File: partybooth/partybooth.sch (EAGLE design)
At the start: 21 parts, among them IC1 TINY13-20PU, IC2 78L05Z, J1 Lamp, J2 Button, J3 12V, T1 2N3904, T2 2N3904, X1 1501_06

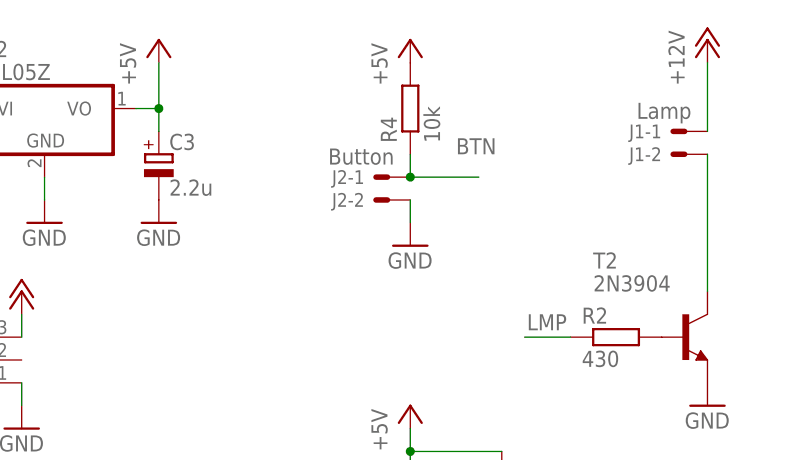
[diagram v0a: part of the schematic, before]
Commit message: 
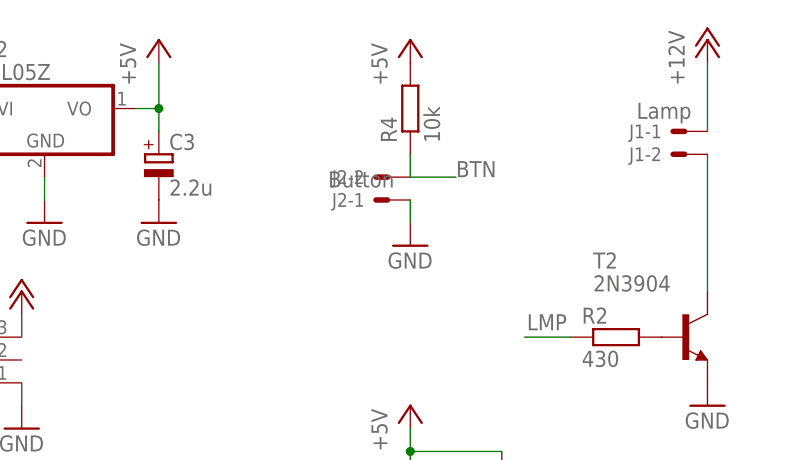
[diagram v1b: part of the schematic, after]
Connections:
- net BTN: now also J2-2.S; no longer J2-1.S
- net GND: now also J2-1.S; no longer J2-2.S
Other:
- moved on the sheet: J2-1, J2-2
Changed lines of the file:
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@@
 <instance part="OK1" gate="A" x="38.1" y="45.72"/>
 <instance part="OK1" gate="B" x="38.1" y="30.48"/>
-<instance part="J2" gate="-1" x="-17.78" y="96.52" rot="MR0"/>
-<instance part="J2" gate="-2" x="-17.78" y="93.98" rot="MR0"/>
+<instance part="J2" gate="-1" x="-17.78" y="93.98" rot="MR0"/>
+<instance part="J2" gate="-2" x="-17.78" y="96.52" rot="MR0"/>
 <instance part="SV1" gate="1" x="5.08" y="48.26" rot="R180"/>
 <instance part="P+4" gate="1" x="15.24" y="58.42"/>
@@
 </segment>
 <segment>
-<pinref part="GND10" gate="1" pin="GND"/>
-<pinref part="J2" gate="-2" pin="S"/>
-<wire x1="-15.24" y1="91.44" x2="-15.24" y2="93.98" width="0.1524" layer="91"/>
-</segment>
-<segment>
 <pinref part="GND11" gate="1" pin="GND"/>
 <pinref part="J3" gate="G$1" pin="1"/>
 <wire x1="-58.42" y1="73.66" x2="-58.42" y2="71.12" width="0.1524" layer="91"/>
+</segment>
+<segment>
+<pinref part="J2" gate="-1" pin="S"/>
+<pinref part="GND10" gate="1" pin="GND"/>
+<wire x1="-15.24" y1="93.98" x2="-15.24" y2="91.44" width="0.1524" layer="91"/>
 </segment>
 </net>
@@
 <net name="BTN" class="0">
 <segment>
-<pinref part="R4" gate="G$1" pin="1"/>
-<wire x1="-15.24" y1="96.52" x2="-15.24" y2="99.06" width="0.1524" layer="91"/>
-<pinref part="J2" gate="-1" pin="S"/>
-<wire x1="-15.24" y1="96.52" x2="-7.62" y2="96.52" width="0.1524" layer="91"/>
-<label x="-10.16" y="99.06" size="1.778" layer="95"/>
-<junction x="-15.24" y="96.52"/>
-</segment>
-<segment>
 <pinref part="IC1" gate="G$1" pin="PB1/PCINT1/AIN1/OC0B/INT0/MISO"/>
 <pinref part="SV1" gate="1" pin="1"/>
@@
 <label x="-15.24" y="51.308" size="1.778" layer="95"/>
 </segment>
-</net>
+<segment>
+<pinref part="R4" gate="G$1" pin="1"/>
+<pinref part="J2" gate="-2" pin="S"/>
+<wire x1="-15.24" y1="99.06" x2="-15.24" y2="96.52" width="0.1524" layer="91"/>
+<wire x1="-15.24" y1="96.52" x2="-10.16" y2="96.52" width="0.1524" layer="91"/>
+<label x="-10.16" y="96.52" size="1.778" layer="95"/>
+</segment>
+</net>

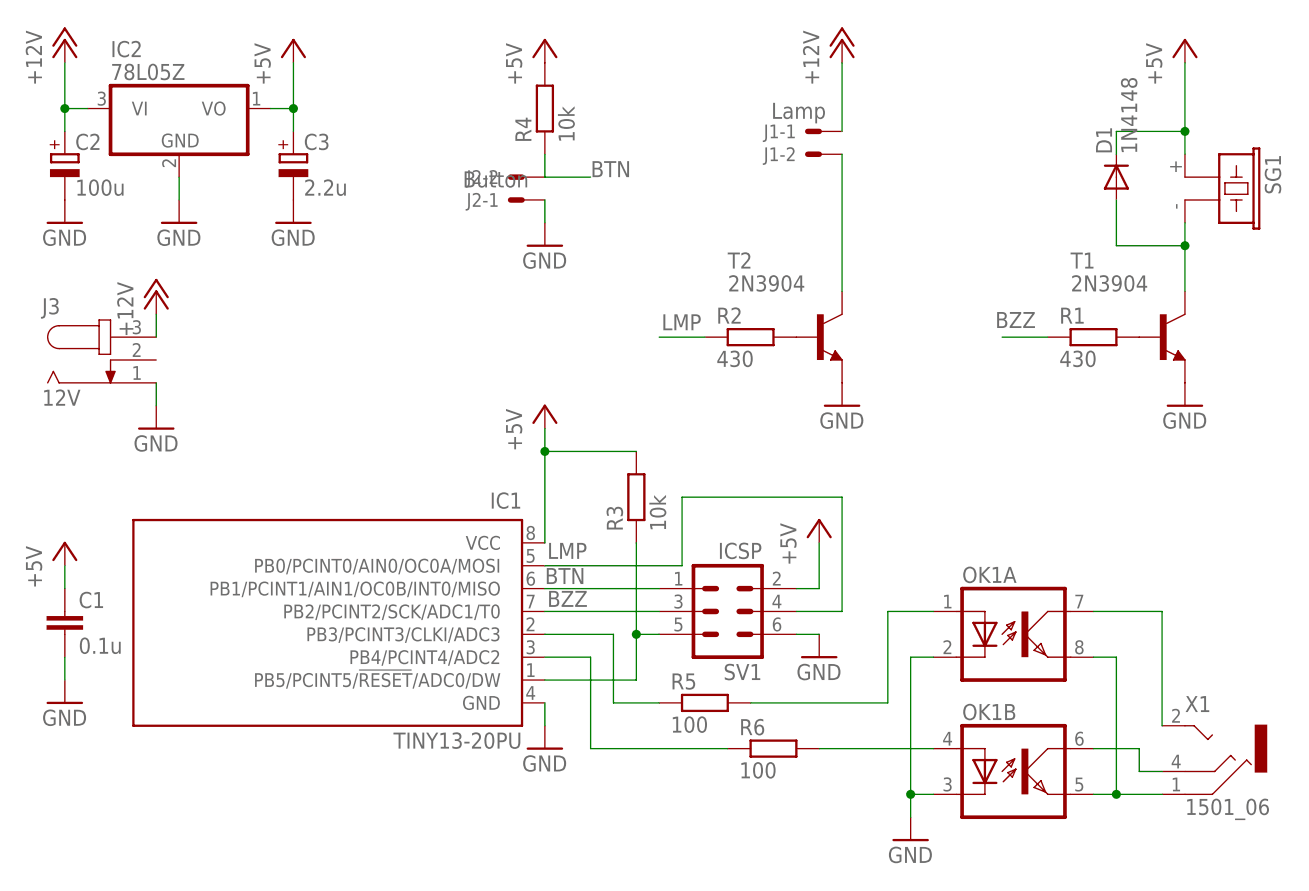
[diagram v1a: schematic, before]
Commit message: 
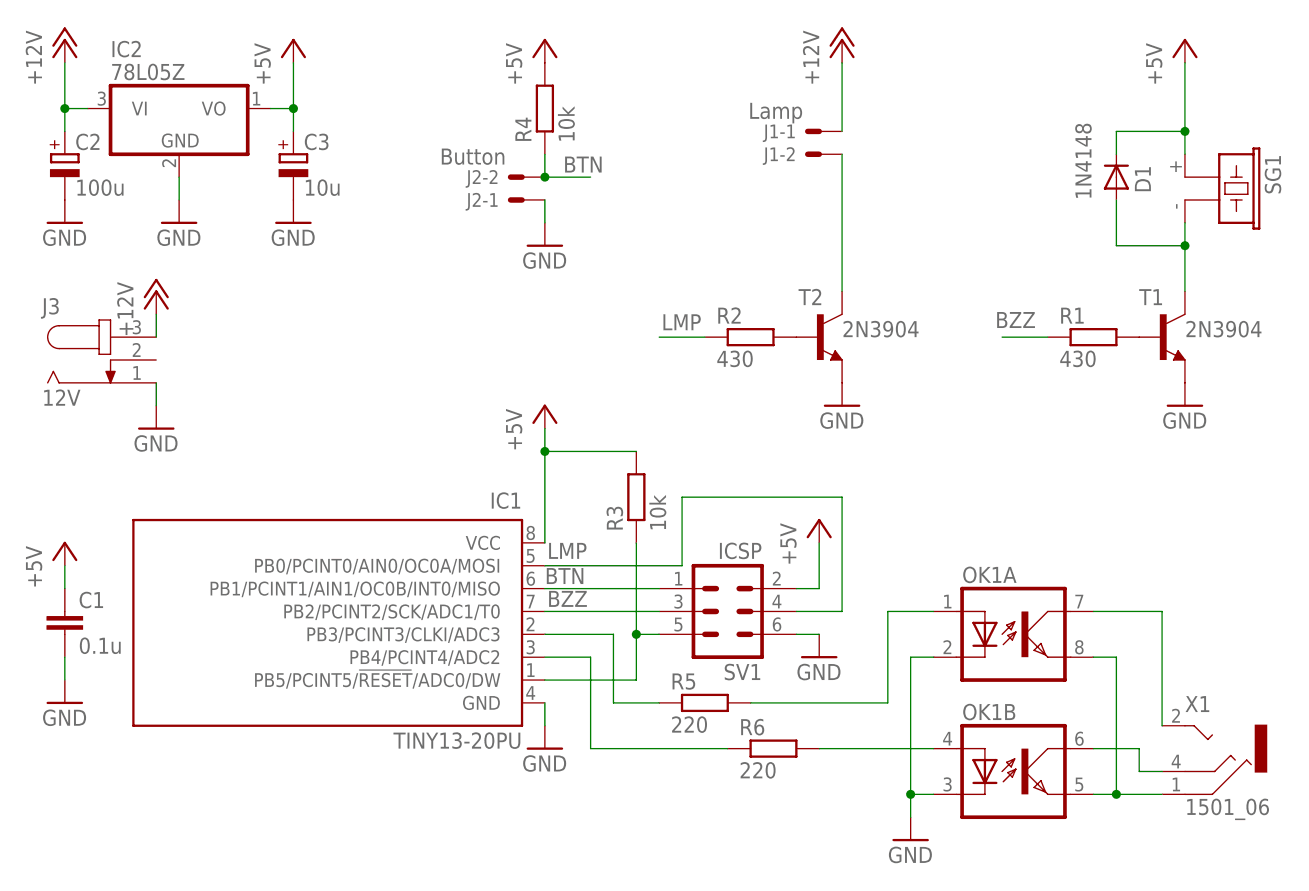
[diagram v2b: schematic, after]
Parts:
- C3: value 2.2u -> 10u
- R5, R6: value 100 -> 220
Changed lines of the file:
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@@
 <layer number="95" name="Names" color="7" fill="1" visible="yes" active="yes"/>
 <layer number="96" name="Values" color="7" fill="1" visible="yes" active="yes"/>
-<layer number="97" name="Info" color="7" fill="1" visible="yes" active="yes"/>
+<layer number="97" name="Info" color="7" fill="1" visible="no" active="yes"/>
 <layer number="98" name="Guide" color="6" fill="1" visible="yes" active="yes"/>
 </layers>
@@
 <part name="IC2" library="linear" deviceset="78*" device="Z" technology="L05"/>
 <part name="C2" library="rcl" deviceset="CPOL-EU" device="B45181B" value="100u"/>
-<part name="C3" library="rcl" deviceset="CPOL-EU" device="B45181B" value="2.2u"/>
+<part name="C3" library="rcl" deviceset="CPOL-EU" device="B45181B" value="10u"/>
 <part name="GND7" library="supply1" deviceset="GND" device=""/>
 <part name="GND8" library="supply1" deviceset="GND" device=""/>
@@
 <part name="P+8" library="supply1" deviceset="+5V" device=""/>
 <part name="GND10" library="supply1" deviceset="GND" device=""/>
-<part name="R5" library="rcl" deviceset="R-EU_" device="0204/7" value="100"/>
-<part name="R6" library="rcl" deviceset="R-EU_" device="0204/7" value="100"/>
+<part name="R5" library="rcl" deviceset="R-EU_" device="0204/7" value="220"/>
+<part name="R6" library="rcl" deviceset="R-EU_" device="0204/7" value="220"/>
 <part name="J3" library="con-jack" deviceset="JACK-PLUG" device="0" value="12V"/>
 <part name="P+9" library="supply1" deviceset="+12V" device=""/>
@@
 <instances>
 <instance part="SG1" gate="G$1" x="58.42" y="96.52" rot="R270"/>
-<instance part="T1" gate="G1" x="53.34" y="78.74"/>
-<instance part="T2" gate="G1" x="15.24" y="78.74"/>
+<instance part="T1" gate="G1" x="53.34" y="78.74" smashed="yes">
+<attribute name="NAME" x="50.8" y="82.296" size="1.778" layer="95"/>
+<attribute name="VALUE" x="55.88" y="78.74" size="1.778" layer="96"/>
+</instance>
+<instance part="T2" gate="G1" x="15.24" y="78.74" smashed="yes">
+<attribute name="NAME" x="12.954" y="82.296" size="1.778" layer="95"/>
+<attribute name="VALUE" x="17.78" y="78.74" size="1.778" layer="96"/>
+</instance>
 <instance part="R1" gate="G$1" x="45.72" y="78.74"/>
 <instance part="GND1" gate="1" x="55.88" y="71.12"/>
 <instance part="P+1" gate="1" x="55.88" y="111.76"/>
-<instance part="D1" gate="G$1" x="48.26" y="96.52" rot="R90"/>
-<instance part="J1" gate="-1" x="15.24" y="101.6" rot="MR0"/>
+<instance part="D1" gate="G$1" x="48.26" y="96.52" smashed="yes" rot="R90">
+<attribute name="NAME" x="52.0954" y="94.742" size="1.778" layer="95" rot="R90"/>
+<attribute name="VALUE" x="45.4914" y="93.98" size="1.778" layer="96" rot="R90"/>
+</instance>
+<instance part="J1" gate="-1" x="15.24" y="101.6" smashed="yes" rot="MR0">
+<attribute name="NAME" x="12.7" y="100.838" size="1.524" layer="95" rot="MR0"/>
+<attribute name="VALUE" x="13.462" y="102.997" size="1.778" layer="96" rot="MR0"/>
+</instance>
 <instance part="J1" gate="-2" x="15.24" y="99.06" rot="MR0"/>
 <instance part="P+2" gate="1" x="17.78" y="111.76"/>
@@
 <instance part="OK1" gate="A" x="38.1" y="45.72"/>
 <instance part="OK1" gate="B" x="38.1" y="30.48"/>
-<instance part="J2" gate="-1" x="-17.78" y="93.98" rot="MR0"/>
+<instance part="J2" gate="-1" x="-17.78" y="93.98" smashed="yes" rot="MR0">
+<attribute name="NAME" x="-20.32" y="93.218" size="1.524" layer="95" rot="MR0"/>
+<attribute name="VALUE" x="-19.558" y="97.917" size="1.778" layer="96" rot="MR0"/>
+</instance>
 <instance part="J2" gate="-2" x="-17.78" y="96.52" rot="MR0"/>
 <instance part="SV1" gate="1" x="5.08" y="48.26" rot="R180"/>
@@
 <pinref part="R4" gate="G$1" pin="1"/>
 <pinref part="J2" gate="-2" pin="S"/>
-<wire x1="-15.24" y1="99.06" x2="-15.24" y2="96.52" width="0.1524" layer="91"/>
 <wire x1="-15.24" y1="96.52" x2="-10.16" y2="96.52" width="0.1524" layer="91"/>
-<label x="-10.16" y="96.52" size="1.778" layer="95"/>
-</segment>
-</net>
+<label x="-13.208" y="97.028" size="1.778" layer="95"/>
+<junction x="-15.24" y="96.52"/>
+<wire x1="-15.24" y1="96.52" x2="-15.24" y2="99.06" width="0.1524" layer="91"/>
+</segment>
+</net>

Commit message: 
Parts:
- C1: device rcl:C-EU025_050-025X075 -> rcl:C-EU050-025X075
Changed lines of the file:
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@@
 <grid distance="0.1" unitdist="inch" unit="inch" style="lines" multiple="1" display="no" altdistance="0.01" altunitdist="inch" altunit="inch"/>
 <layers>
-<layer number="1" name="Top" color="4" fill="1" visible="no" active="no"/>
-<layer number="2" name="Route2" color="1" fill="3" visible="no" active="no"/>
-<layer number="3" name="Route3" color="4" fill="3" visible="no" active="no"/>
-<layer number="14" name="Route14" color="1" fill="6" visible="no" active="no"/>
-<layer number="15" name="Route15" color="4" fill="6" visible="no" active="no"/>
-<layer number="16" name="Bottom" color="1" fill="1" visible="no" active="no"/>
-<layer number="17" name="Pads" color="2" fill="1" visible="no" active="no"/>
-<layer number="18" name="Vias" color="2" fill="1" visible="no" active="no"/>
-<layer number="19" name="Unrouted" color="6" fill="1" visible="no" active="no"/>
-<layer number="20" name="Dimension" color="15" fill="1" visible="no" active="no"/>
-<layer number="21" name="tPlace" color="7" fill="1" visible="no" active="no"/>
-<layer number="22" name="bPlace" color="7" fill="1" visible="no" active="no"/>
-<layer number="23" name="tOrigins" color="15" fill="1" visible="no" active="no"/>
-<layer number="24" name="bOrigins" color="15" fill="1" visible="no" active="no"/>
-<layer number="25" name="tNames" color="7" fill="1" visible="no" active="no"/>
-<layer number="26" name="bNames" color="7" fill="1" visible="no" active="no"/>
-<layer number="27" name="tValues" color="7" fill="1" visible="no" active="no"/>
-<layer number="28" name="bValues" color="7" fill="1" visible="no" active="no"/>
+<layer number="1" name="Top" color="4" fill="1" visible="yes" active="no"/>
+<layer number="2" name="Route2" color="1" fill="3" visible="yes" active="no"/>
+<layer number="3" name="Route3" color="4" fill="3" visible="yes" active="no"/>
+<layer number="14" name="Route14" color="1" fill="6" visible="yes" active="no"/>
+<layer number="15" name="Route15" color="4" fill="6" visible="yes" active="no"/>
+<layer number="16" name="Bottom" color="1" fill="1" visible="yes" active="no"/>
+<layer number="17" name="Pads" color="2" fill="1" visible="yes" active="no"/>
+<layer number="18" name="Vias" color="2" fill="1" visible="yes" active="no"/>
+<layer number="19" name="Unrouted" color="6" fill="1" visible="yes" active="no"/>
+<layer number="20" name="Dimension" color="15" fill="1" visible="yes" active="no"/>
+<layer number="21" name="tPlace" color="7" fill="1" visible="yes" active="no"/>
+<layer number="22" name="bPlace" color="7" fill="1" visible="yes" active="no"/>
+<layer number="23" name="tOrigins" color="15" fill="1" visible="yes" active="no"/>
+<layer number="24" name="bOrigins" color="15" fill="1" visible="yes" active="no"/>
+<layer number="25" name="tNames" color="7" fill="1" visible="yes" active="no"/>
+<layer number="26" name="bNames" color="7" fill="1" visible="yes" active="no"/>
+<layer number="27" name="tValues" color="7" fill="1" visible="yes" active="no"/>
+<layer number="28" name="bValues" color="7" fill="1" visible="yes" active="no"/>
 <layer number="29" name="tStop" color="7" fill="3" visible="no" active="no"/>
 <layer number="30" name="bStop" color="7" fill="6" visible="no" active="no"/>
@@
 <layer number="35" name="tGlue" color="7" fill="4" visible="no" active="no"/>
 <layer number="36" name="bGlue" color="7" fill="5" visible="no" active="no"/>
-<layer number="37" name="tTest" color="7" fill="1" visible="no" active="no"/>
-<layer number="38" name="bTest" color="7" fill="1" visible="no" active="no"/>
+<layer number="37" name="tTest" color="7" fill="1" visible="yes" active="no"/>
+<layer number="38" name="bTest" color="7" fill="1" visible="yes" active="no"/>
 <layer number="39" name="tKeepout" color="4" fill="11" visible="no" active="no"/>
 <layer number="40" name="bKeepout" color="1" fill="11" visible="no" active="no"/>
@@
 <layer number="44" name="Drills" color="7" fill="1" visible="no" active="no"/>
 <layer number="45" name="Holes" color="7" fill="1" visible="no" active="no"/>
-<layer number="46" name="Milling" color="3" fill="1" visible="no" active="no"/>
-<layer number="47" name="Measures" color="7" fill="1" visible="no" active="no"/>
-<layer number="48" name="Document" color="7" fill="1" visible="no" active="no"/>
-<layer number="49" name="Reference" color="7" fill="1" visible="no" active="no"/>
-<layer number="51" name="tDocu" color="6" fill="1" visible="no" active="no"/>
-<layer number="52" name="bDocu" color="7" fill="1" visible="no" active="no"/>
+<layer number="46" name="Milling" color="3" fill="1" visible="yes" active="no"/>
+<layer number="47" name="Measures" color="7" fill="1" visible="yes" active="no"/>
+<layer number="48" name="Document" color="7" fill="1" visible="yes" active="no"/>
+<layer number="49" name="Reference" color="7" fill="1" visible="yes" active="no"/>
+<layer number="51" name="tDocu" color="7" fill="1" visible="yes" active="no"/>
+<layer number="52" name="bDocu" color="7" fill="1" visible="yes" active="no"/>
 <layer number="91" name="Nets" color="2" fill="1" visible="yes" active="yes"/>
 <layer number="92" name="Busses" color="1" fill="1" visible="yes" active="yes"/>
@@
 <part name="P+4" library="supply1" deviceset="+5V" device=""/>
 <part name="GND4" library="supply1" deviceset="GND" device=""/>
-<part name="C1" library="rcl" deviceset="C-EU" device="025_050-025X075" value="0.1u"/>
+<part name="C1" library="rcl" deviceset="C-EU" device="050-025X075" value="0.1u"/>
 <part name="GND5" library="supply1" deviceset="GND" device=""/>
 <part name="P+5" library="supply1" deviceset="+5V" device=""/>
